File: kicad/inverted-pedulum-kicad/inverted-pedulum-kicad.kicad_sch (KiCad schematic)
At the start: 8 parts, among them M1 Stepper_Motor_bipolar (17HS16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, SW1 SW_DPST, U1 ARDUIO_DUE_R3, U2 ERCK_0505_360, U3 TB6600

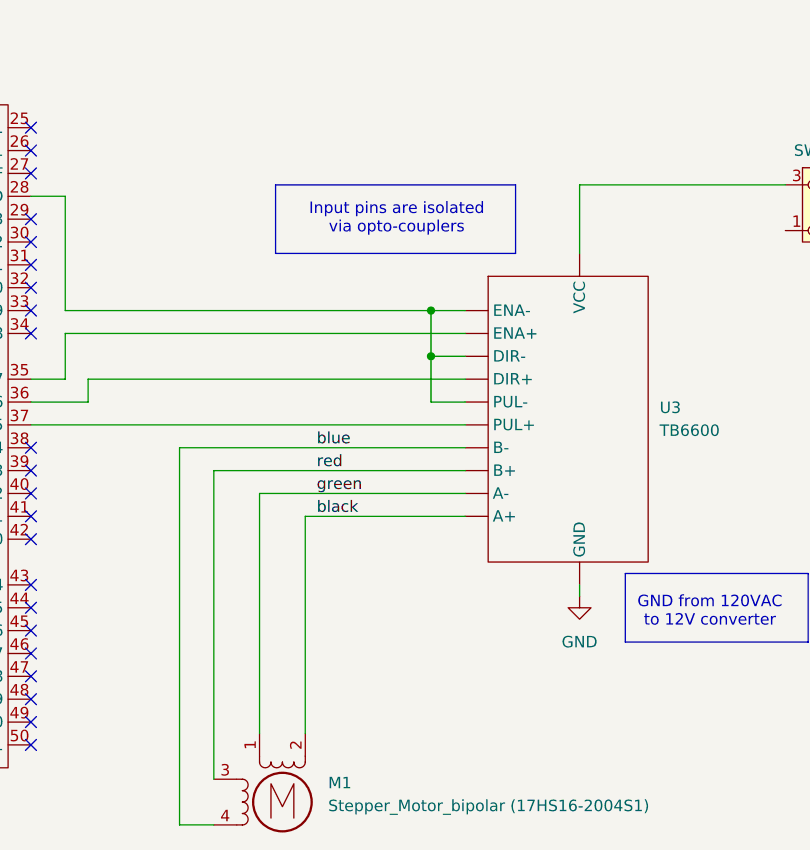
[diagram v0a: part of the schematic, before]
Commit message: feat: updates to schematics
- fixed stepper wiring
- updated title block
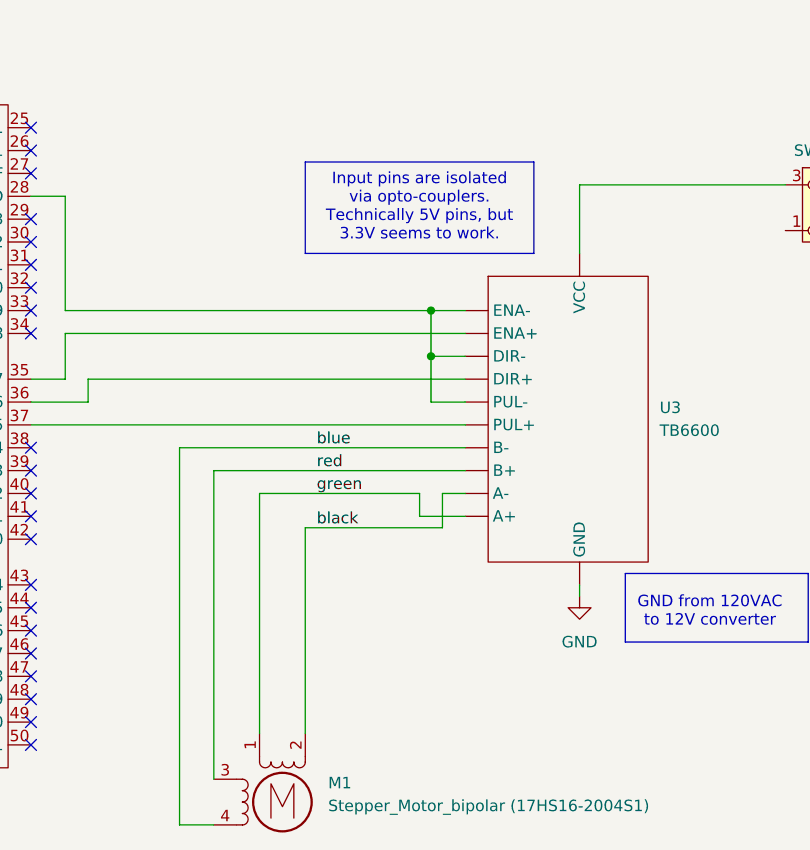
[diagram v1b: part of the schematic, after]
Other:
- note added: "Input pins are isolated via opto-couplers. Technically 5V pins, but 3.3V seems to work."
- note removed: "Input pins are isolated via opto-couplers"
- title: (none) -> Inverted Pendulum
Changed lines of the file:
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@@
 	(generator_version "9.0")
 	(paper "A4")
+	(title_block
+		(title "Inverted Pendulum")
+		(date "2026-02-04")
+		(rev "1")
+	)
 	(rectangle
-		(start 171.958 60.96)
-		(end 198.628 68.58)
+		(start 175.26 58.42)
+		(end 200.66 68.58)
 		(stroke
 			(width 0)
@@
 		)
 	)
-	(text "Input pins are isolated\nvia opto-couplers"
+	(text "Input pins are isolated\nvia opto-couplers.\nTechnically 5V pins, but\n3.3V seems to work."
 		(exclude_from_sim no)
-		(at 185.42 64.77 0)
+		(at 187.96 63.5 0)
 		(effects
 			(font
@@
 	(wire
 		(pts
+			(xy 190.5 95.25) (xy 190.5 99.06)
+		)
+		(stroke
+			(width 0)
+			(type default)
+		)
+	)
+	(wire
+		(pts
 			(xy 170.18 121.92) (xy 170.18 95.25)
 		)
@@
 	(wire
 		(pts
+			(xy 190.5 95.25) (xy 193.04 95.25)
+		)
+		(stroke
+			(width 0)
+			(type default)
+		)
+	)
+	(wire
+		(pts
 			(xy 60.96 107.95) (xy 60.96 104.14)
 		)
@@
 	(wire
 		(pts
-			(xy 175.26 121.92) (xy 175.26 97.79)
+			(xy 187.96 95.25) (xy 187.96 97.79)
 		)
 		(stroke
@@
 	(wire
 		(pts
+			(xy 187.96 97.79) (xy 193.04 97.79)
+		)
+		(stroke
+			(width 0)
+			(type default)
+		)
+	)
+	(wire
+		(pts
 			(xy 60.96 76.2) (xy 60.96 64.77)
 		)
@@
 	(wire
 		(pts
-			(xy 170.18 95.25) (xy 193.04 95.25)
-		)
-		(stroke
-			(width 0)
-			(type default)
-		)
-	)
-	(wire
-		(pts
-			(xy 175.26 97.79) (xy 193.04 97.79)
+			(xy 170.18 95.25) (xy 187.96 95.25)
+		)
+		(stroke
+			(width 0)
+			(type default)
+		)
+	)
+	(wire
+		(pts
+			(xy 175.26 99.06) (xy 190.5 99.06)
 		)
 		(stroke
@@
 		(pts
 			(xy 205.74 60.96) (xy 205.74 68.58)
+		)
+		(stroke
+			(width 0)
+			(type default)
+		)
+	)
+	(wire
+		(pts
+			(xy 175.26 99.06) (xy 175.26 121.92)
 		)
 		(stroke
@@
 	)
 	(label "black"
-		(at 176.53 97.79 0)
-		(effects
-			(font
+		(at 176.53 99.06 0)
+		(effects
+			(font
